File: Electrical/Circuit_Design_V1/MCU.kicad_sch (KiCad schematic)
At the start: 0 parts

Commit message: #3 Sourcing capacitors, and designing power for MCU.
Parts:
- added C10, C8: 1uF, symbol Device:C
- added C2, C3, C4, C5, C9: 100nF, symbol Device:C
- added C6: 10nF, symbol Device:C
- added C7: 4.7uF, symbol Device:C
- added U1: STM32G474RETx, Package_QFP:LQFP-64_10x10mm_P0.5mm, symbol MCU_ST_STM32G4:STM32G474RETx
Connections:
- new net: C3.2, U1.32 (VDD)
- new net: C4.2, U1.16 (VDD)
- new net: C5.2, U1.64 (VDD)
- new net: C6.2, U1.29 (VDDA)
- new net: C2.2, U1.48 (VDD)
- new net +3V3: C10.1, C7.2, C8.1, C9.2, U1.1 (VBAT), U1.28 (VREF+)
- new net GND: C10.2, C2.1, C3.1, C4.1, C5.1, C6.1, C7.1, C8.2, C9.1, U1.15 (VSS), U1.27 (VSSA), U1.31 (VSS), U1.47 (VSS), U1.63 (VSS)
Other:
- note added: "For VDD-VSS Pair"
- note added: "For VDDA-VSSA Pair"
- note added: "When designing the layout, capacitors should remain as close to the MCU's pins as reasonably possible."
- company: (none) -> AdrianTheHacker
- title: (none) -> MCU

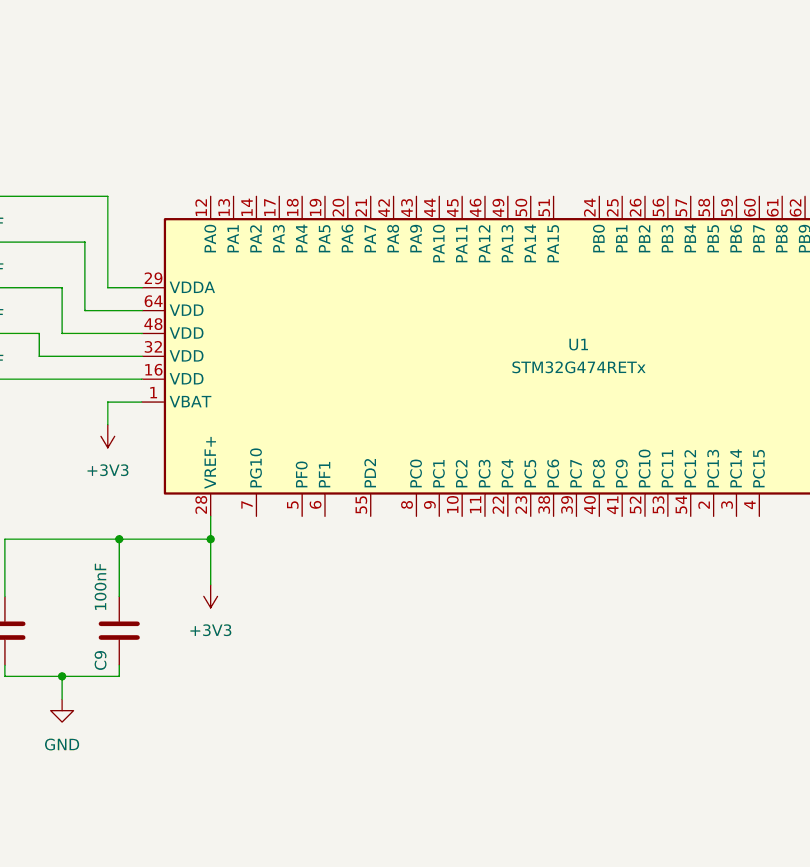
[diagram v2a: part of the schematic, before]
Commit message: #3 Adding accelerometer to schematic.
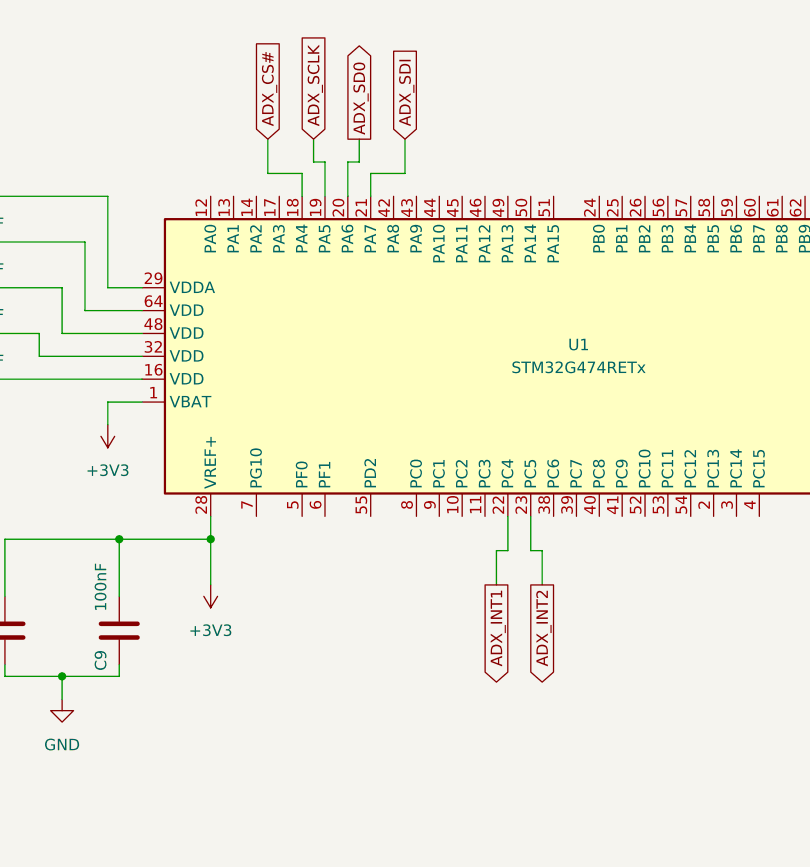
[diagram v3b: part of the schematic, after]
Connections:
- net ADX_CS#: now reaches U1.18 (PA4)
- net ADX_SCLK: now reaches U1.19 (PA5)
- net ADX_SD0: now reaches U1.20 (PA6)
- net ADX_SDI: now reaches U1.21 (PA7)
- net ADX_INT1: now reaches U1.22 (PC4)
- net ADX_INT2: now reaches U1.23 (PC5)
